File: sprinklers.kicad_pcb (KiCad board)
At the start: 2 copper layers, 144.3 x 152.4 mm, 69 parts, among them J1 Conn_01x02, J2 Conn_01x02, J3 Conn_01x02, J4 Conn_01x02, J5 Conn_01x02, J6 Conn_01x02, K1 SANYOU_SRD_Form_C, K2 SANYOU_SRD_Form_C, K3 SANYOU_SRD_Form_C, K4 SANYOU_SRD_Form_C, K5 SANYOU_SRD_Form_C, K6 SANYOU_SRD_Form_C, Q1 Q_NMOS_GDS, Q2 Q_NMOS_GDS, Q3 Q_NMOS_GDS, Q4 Q_NMOS_GDS, Q5 Q_NMOS_GDS, Q6 Q_NMOS_GDS, U1 LM2596S-5, U2 AP1117-33, U2 ESP32-WROOM-32D, U3 AP1117-33, U3 ESP32-WROOM-32D

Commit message: V1.1.0 with notation
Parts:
- removed 12V-IN, SENSOR: Conn_01x02, Connector:JWT_A3963_1x02_P3.96mm_Vertical
- removed BOOT: SW_SPST, Button_Switch_SMD:SW_Push_1P1T_NO_Vertical_Wuerth_434133025816
- removed the C1 at (105.4, 79.2)
- removed the C1 at (46.0, 147.5)
- removed the C2 at (46.0, 148.7)
- removed the C2 at (106.7, 79.2)
- removed the C3 at (119.4, 78.7)
- removed the C3 at (41.8, 162.4)
- removed the C4 at (120.7, 78.7)
- removed the C4 at (43.1, 162.4)
- removed the C5 at (47.0, 90.6)
- removed the C5 at (27.5, 142.4)
- removed the C6 at (55.9, 84.3)
- removed the C6 at (25.7, 153.5)
- removed the D1 at (128.1, 38.1)
- removed the D1 at (34.1, 132.2)
- removed the D2 at (128.1, 35.6)
- removed the D2 at (33.6, 139.8)
- removed the D3 at (128.1, 33.0)
- removed the D3 at (60.8, 141.1)
- removed the D4 at (58.2, 141.1)
- removed the D4 at (45.7, 80.5)
- removed the D5 at (55.9, 141.1)
- removed the D5 at (55.9, 90.6)
- removed the EXT/PROG at (65.9, 131.0)
- removed the EXT/PROG at (143.5, 66.0)
- removed GND 5V 3V3: PinHeader_1x03_P2.54mm_Vertical, Connector_PinHeader_2.54mm:PinHeader_1x03_P2.54mm_Vertical
- removed the L1 at (37.3, 152.8)
- removed the L1 at (89.5, 88.0)
- removed the R1 at (33.1, 43.2)
- removed the R1 at (60.7, 137.3)
- removed the R2 at (58.3, 137.3)
- removed the R2 at (50.2, 43.2)
- removed the R3 at (55.8, 137.3)
- removed the R3 at (68.6, 43.2)
- removed the R7 at (123.0, 33.0)
- removed the R8 at (123.0, 35.6)
- removed the R9 at (123.0, 38.1)
- removed the U1 at (74.6, 89.1)
- removed the U1 at (43.3, 135.1)
- removed the U2 at (145.4, 42.0)
- removed the U2 at (35.4, 164.0)
- removed the U3 at (113.6, 81.3)
- removed the U3 at (61.4, 154.4)
- added 7  6  5  G: PinHeader_1x04_P2.54mm_Vertical, Connector_PinHeader_2.54mm:PinHeader_1x04_P2.54mm_Vertical, F.Cu at (148.5, 22.8)
- added ?: , , F.Cu at (41.0, 166.8)
- added ?: LOGO, my lib:sprinklers qr code, B.Cu at (40.3, 169.5)
- added ?: LOGO, my lib:sprinklers qr code, B.Cu at (90.2, 38.1)
- added ?: , , F.Cu at (43.5, 166.8)
- added ?: , , F.Cu at (41.0, 124.8)
- added ?: , , F.Cu at (38.4, 166.8)
- added ?: , , F.Cu at (141.0, 65.2)
- added ?: , , F.Cu at (43.5, 124.8)
- added ?: , , F.Cu at (38.5, 124.8)
- added ?: , , F.Cu at (130.7, 25.4)
- added ?: LOGO, my lib:sprinklers qr code, B.Cu at (40.3, 127.4)
- added AC12-IN1: Conn_01x02, Connector:JWT_A3963_1x02_P3.96mm_Vertical, F.Cu at (73.0, 137.6)
- added AC12-IN1: Conn_01x02, Connector:JWT_A3963_1x02_P3.96mm_Vertical, F.Cu at (73.0, 179.6)
- added C1: 10uF, Capacitor_SMD:C_0805_2012Metric, F.Cu at (36.9, 132.5)
- added C1: 10uF, Capacitor_SMD:C_0805_2012Metric, F.Cu at (36.9, 174.5)
- added C1: 10uF, Capacitor_SMD:C_0805_2012Metric, F.Cu at (102.9, 75.5)
- added C2: 100nF, Capacitor_SMD:C_0603_1608Metric, F.Cu at (39.6, 132.5)
- added C2: 100nF, Capacitor_SMD:C_0603_1608Metric, F.Cu at (39.6, 174.5)
- added C2: 100nF, Capacitor_SMD:C_0603_1608Metric, F.Cu at (104.8, 76.2)
- added C3: 10uF, Capacitor_SMD:C_0805_2012Metric, F.Cu at (116.8, 75.7)
- added C3: 10uF, Capacitor_SMD:C_0805_2012Metric, F.Cu at (36.9, 136.6)
- added C3: 10uF, Capacitor_SMD:C_0805_2012Metric, F.Cu at (36.9, 178.7)
- added C4: 100nF, Capacitor_SMD:C_0603_1608Metric, F.Cu at (39.7, 178.7)
- added C4: 100nF, Capacitor_SMD:C_0603_1608Metric, F.Cu at (119.4, 75.1)
- added C4: 100nF, Capacitor_SMD:C_0603_1608Metric, F.Cu at (39.7, 136.7)
- added C5: C_Polarized, Capacitor_THT:CP_Radial_D8.0mm_P3.50mm, F.Cu at (45.7, 88.4)
- added C5: C_Polarized, Capacitor_THT:CP_Radial_D8.0mm_P3.50mm, F.Cu at (73.7, 116.8)
- added C5: C_Polarized, Capacitor_THT:CP_Radial_D8.0mm_P3.50mm, F.Cu at (73.7, 158.8)
- added C6: C_Polarized, Capacitor_THT:CP_Radial_D8.0mm_P3.50mm, F.Cu at (63.6, 167.7)
- added C6: C_Polarized, Capacitor_THT:CP_Radial_D8.0mm_P3.50mm, F.Cu at (53.3, 81.0)
- added C6: C_Polarized, Capacitor_THT:CP_Radial_D8.0mm_P3.50mm, F.Cu at (63.6, 125.7)
- added D1: LED, LED_SMD:LED_0402_1005Metric, F.Cu at (125.6, 34.8)
- added D1: LED, LED_SMD:LED_0402_1005Metric, F.Cu at (27.2, 166.4)
- added D1: LED, LED_SMD:LED_0402_1005Metric, F.Cu at (27.2, 124.4)
- added D2: LED, LED_SMD:LED_0402_1005Metric, F.Cu at (125.6, 32.3)
- added D2: LED, LED_SMD:LED_0402_1005Metric, F.Cu at (33.1, 166.4)
- added D2: LED, LED_SMD:LED_0402_1005Metric, F.Cu at (33.1, 124.4)
- added D3: LED, LED_SMD:LED_0402_1005Metric, F.Cu at (125.6, 29.7)
- added D3: LED, LED_SMD:LED_0402_1005Metric, F.Cu at (29.8, 124.4)
- added D3: LED, LED_SMD:LED_0402_1005Metric, F.Cu at (29.8, 166.4)
- added D4: 900mV@2A 30ns 2A 50V DO-214AA Diodes, Diode_SMD:D_SMB, F.Cu at (63.6, 179.1)
- added D4: 900mV@2A 30ns 2A 50V DO-214AA Diodes, Diode_SMD:D_SMB, F.Cu at (63.6, 137.1)
- added D4: 900mV@2A 30ns 2A 50V DO-214AA Diodes, Diode_SMD:D_SMB, F.Cu at (33.8, 79.2)
- added D5: B140-E3, Diode_SMD:D_SMA, F.Cu at (55.9, 163.2)
- added D5: B140-E3, Diode_SMD:D_SMA, F.Cu at (53.3, 87.3)
- added D5: B140-E3, Diode_SMD:D_SMA, F.Cu at (56.0, 121.1)
- added D6: 900mV@2A 30ns 2A 50V DO-214AA Diodes, Diode_SMD:D_SMB, F.Cu at (33.8, 75.4)
- added D6: 900mV@2A 30ns 2A 50V DO-214AA Diodes, Diode_SMD:D_SMB, F.Cu at (63.6, 173.2)
- added D6: 900mV@2A 30ns 2A 50V DO-214AA Diodes, Diode_SMD:D_SMB, F.Cu at (63.6, 131.1)
- added D7: 900mV@2A 30ns 2A 50V DO-214AA Diodes, Diode_SMD:D_SMB, F.Cu at (70.8, 127.5)
- added D7: 900mV@2A 30ns 2A 50V DO-214AA Diodes, Diode_SMD:D_SMB, F.Cu at (39.4, 84.9)
- added D7: 900mV@2A 30ns 2A 50V DO-214AA Diodes, Diode_SMD:D_SMB, F.Cu at (70.8, 169.5)
- added D8: 900mV@2A 30ns 2A 50V DO-214AA Diodes, Diode_SMD:D_SMB, F.Cu at (76.3, 127.5)
- added D8: 900mV@2A 30ns 2A 50V DO-214AA Diodes, Diode_SMD:D_SMB, F.Cu at (44.5, 81.8)
- added D8: 900mV@2A 30ns 2A 50V DO-214AA Diodes, Diode_SMD:D_SMB, F.Cu at (76.3, 169.5)
- added EXT/PROG: PinHeader_2x03_P1.27mm_Vertical, Connector_PinHeader_1.27mm:PinHeader_2x03_P1.27mm_Vertical, F.Cu at (48.6, 109.6)
- added EXT/PROG: PinHeader_2x03_P1.27mm_Vertical, Connector_PinHeader_1.27mm:PinHeader_2x03_P1.27mm_Vertical, F.Cu at (141.0, 62.7)
- added EXT/PROG: PinHeader_2x03_P1.27mm_Vertical, Connector_PinHeader_1.27mm:PinHeader_2x03_P1.27mm_Vertical, F.Cu at (48.6, 151.6)
- added L1: L, Inductor_SMD:L_12x12mm_H8mm, F.Cu at (61.3, 151.3)
- added L1: L, Inductor_SMD:L_12x12mm_H8mm, F.Cu at (61.3, 109.3)
- added L1: L, Inductor_SMD:L_12x12mm_H8mm, F.Cu at (87.0, 84.7)
- added R1: 1K, Resistor_SMD:R_1206_3216Metric, F.Cu at (30.5, 39.9)
- added R11: 130, Resistor_SMD:R_1206_3216Metric, F.Cu at (130.7, 23.9)
- added R12: 130, Resistor_SMD:R_1206_3216Metric, F.Cu at (133.2, 23.9)
- added R13: 130, Resistor_SMD:R_1206_3216Metric, F.Cu at (135.8, 23.9)
- added R2: 1K, Resistor_SMD:R_1206_3216Metric, F.Cu at (47.7, 39.9)
- added R3: 1K, Resistor_SMD:R_1206_3216Metric, F.Cu at (66.0, 39.9)
- added R7: 130, Resistor_SMD:R_1206_3216Metric, F.Cu at (120.5, 29.7)
- added R7: 130, Resistor_SMD:R_1206_3216Metric, F.Cu at (30.5, 170.3)
- added R7: 130, Resistor_SMD:R_1206_3216Metric, F.Cu at (30.6, 128.2)
- added R8: 130, Resistor_SMD:R_1206_3216Metric, F.Cu at (33.9, 128.2)
- added R8: 130, Resistor_SMD:R_1206_3216Metric, F.Cu at (33.8, 170.3)
- added R8: 130, Resistor_SMD:R_1206_3216Metric, F.Cu at (120.5, 32.3)
- added R9: 130, Resistor_SMD:R_1206_3216Metric, F.Cu at (27.3, 170.3)
- added R9: 130, Resistor_SMD:R_1206_3216Metric, F.Cu at (120.5, 34.8)
- added R9: 130, Resistor_SMD:R_1206_3216Metric, F.Cu at (27.3, 128.2)
- added RV1: R_Potentiometer_Small, Potentiometer_THT:Potentiometer_Bourns_3296Y_Vertical, F.Cu at (127.0, 78.0)
- added RV1: R_Potentiometer_Small, Potentiometer_THT:Potentiometer_Bourns_3296Y_Vertical, F.Cu at (71.5, 147.8)
- added RV1: R_Potentiometer_Small, Potentiometer_THT:Potentiometer_Bourns_3296Y_Vertical, F.Cu at (71.5, 105.7)
- added SENSOR1: Conn_01x02, Connector:JWT_A3963_1x02_P3.96mm_Vertical, F.Cu at (152.8, 79.0)
- added U1: LM2596S-5, Package_TO_SOT_SMD:TO-263-5_TabPin3, F.Cu at (48.6, 132.0)
- added U1: LM2596S-5, Package_TO_SOT_SMD:TO-263-5_TabPin3, F.Cu at (72.0, 85.8)
- added U1: LM2596S-5, Package_TO_SOT_SMD:TO-263-5_TabPin3, F.Cu at (48.6, 174.1)
- added U2: ESP32-WROOM-32D, RF_Module:ESP32-WROOM-32D, F.Cu at (34.4, 153.6)
- added U2: ESP32-WROOM-32D, RF_Module:ESP32-WROOM-32D, F.Cu at (34.5, 111.6)
- added U2: ESP32-WROOM-32D, RF_Module:ESP32-WROOM-32D, F.Cu at (142.9, 38.7)
- added U3: AP1117-33, Package_TO_SOT_SMD:SOT-223-3_TabPin2, F.Cu at (111.1, 78.0)
- added U3: AP1117-33, Package_TO_SOT_SMD:SOT-223-3_TabPin2, F.Cu at (30.5, 177.9)
- added U3: AP1117-33, Package_TO_SOT_SMD:SOT-223-3_TabPin2, F.Cu at (30.6, 135.8)
- moved 26 27 28 29 11.5 mm to (135.2, 50.9), turned to 0 degrees
- moved J1 7.52 mm to (99.3, 87.4)
- moved J2 7.52 mm to (108.9, 87.4)
- moved J3 7.52 mm to (118.5, 87.4)
- moved J4 7.52 mm to (128.1, 87.4)
- moved J5 7.52 mm to (137.7, 87.4)
- moved J6 7.52 mm to (147.3, 87.4)
- moved 5V 3V3 GND 4.18 mm to (143.5, 71.6)
- moved K4 4.17 mm to (89.2, 52.4)
- moved K6 4.17 mm to (124.5, 52.4)
- moved Q3 4.17 mm to (69.4, 44.7)
- moved Q5 4.17 mm to (104.4, 44.7)
- moved K1 4.17 mm to (36.2, 52.4)
- moved K2 4.17 mm to (53.8, 52.4)
- moved Q4 4.17 mm to (86.8, 45.0)
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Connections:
- 26 27 28 29 pad 1: unconnected-(U2-IO5-Pad29) -> (no net)
- 26 27 28 29 pad 2: unconnected-(U2-IO17-Pad28) -> (no net)
- 26 27 28 29 pad 3: unconnected-(U2-IO16-Pad27) -> (no net)
- 26 27 28 29 pad 4: unconnected-(U2-IO4-Pad26) -> (no net)
- 5V 3V3 GND pad 1: GND1 -> (no net)
- 5V 3V3 GND pad 2: Net-(U2-VDD) -> (no net)
- 5V 3V3 GND pad 3: DC5V -> (no net)
- AC24-IN1 pad 2: GND1 -> Net-(AC24-IN1-Pin_2)
- K1 pad 5: DC5V -> Net-(U1-FB)
- K2 pad 5: DC5V -> Net-(U1-FB)
- K3 pad 5: DC5V -> Net-(U1-FB)
- K4 pad 5: DC5V -> Net-(U1-FB)
- K5 pad 5: DC5V -> Net-(U1-FB)
- K6 pad 5: DC5V -> Net-(U1-FB)
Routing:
- net Net-(SENSOR1-Pin_2): track 0.00 -> 566.6 mm, vias 0 -> 22
- net Net-(SENSOR1-Pin_1): track 0.00 -> 445.9 mm, vias 0 -> 24
- net Net-(U1-FB): track 0.00 -> 389.0 mm, vias 0 -> 6
- net DC5V: track 254.9 -> 0.00 mm, vias 2 -> 0
- net Net-(AC24-IN1-Pin_2): track 0.00 -> 183.7 mm
- net GND1: track 896.5 -> 1060.1 mm, vias 1 -> 7
- net Net-(D5-K): track 66.5 -> 222.3 mm
- net (no net): track 358.7 -> 228.4 mm, vias 13 -> 2
- net Net-(D4-K): track 42.5 -> 143.7 mm
- net Net-(U2-VDD): track 95.1 -> 0.00 mm, vias 2 -> 0
- net Net-(D1-A): track 7.62 -> 50.1 mm, vias 0 -> 4
- net Net-(AC12-IN1-Pin_1): track 0.00 -> 35.0 mm
- net Net-(AC12-IN1-Pin_2): track 0.00 -> 20.7 mm
- net Net-(D2-K): track 28.5 -> 8.06 mm, vias 2 -> 0
- net Net-(D1-K): track 28.5 -> 8.21 mm
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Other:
- board size 144.3 x 152.4 mm -> 147.4 x 171.8 mm
- board text added: "<-- V-CUT"
- board text added: "P11"
- board text added: "P12"
- board text added: "TheDontKnowGuy"
- board text added: "These are 2 duplicats of the main board minus the 6x relays."
- board text removed: "GIDEONI"
- board text removed: "GRD AC vs DC https://rayshobby.net/wordpress/24vac-to-5vdc-conversion/"

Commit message: applying fixed after review
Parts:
- removed 26 27 28 29: PinHeader_1x04_P2.54mm_Vertical, Connector_PinHeader_2.54mm:PinHeader_1x04_P2.54mm_Vertical
- removed 5V 3V3 GND: PinHeader_1x03_P2.54mm_Vertical, Connector_PinHeader_2.54mm:PinHeader_1x03_P2.54mm_Vertical
- removed 7  6  5  G: PinHeader_1x04_P2.54mm_Vertical, Connector_PinHeader_2.54mm:PinHeader_1x04_P2.54mm_Vertical
- removed ? (x8): , 
- removed ? (x3): LOGO, my lib:sprinklers qr code
- removed AC12-IN1 (x2): Conn_01x02, Connector:JWT_A3963_1x02_P3.96mm_Vertical
- removed the C1 at (36.9, 132.5)
- removed the C1 at (36.9, 174.5)
- removed the C2 at (39.6, 132.5)
- removed the C2 at (39.6, 174.5)
- removed the C3 at (36.9, 136.6)
- removed the C3 at (36.9, 178.7)
- removed the C4 at (39.7, 178.7)
- removed the C4 at (39.7, 136.7)
- removed the C5 at (73.7, 116.8)
- removed the C5 at (73.7, 158.8)
- removed the C6 at (63.6, 167.7)
- removed the C6 at (63.6, 125.7)
- removed the D1 at (27.2, 166.4)
- removed the D1 at (27.2, 124.4)
- removed the D2 at (33.1, 166.4)
- removed the D2 at (33.1, 124.4)
- removed the D3 at (29.8, 124.4)
- removed the D3 at (29.8, 166.4)
- removed the D4 at (63.6, 179.1)
- removed the D4 at (63.6, 137.1)
- removed the D5 at (55.9, 163.2)
- removed the D5 at (56.0, 121.1)
- removed the D6 at (63.6, 173.2)
- removed the D6 at (63.6, 131.1)
- removed the D7 at (70.8, 127.5)
- removed the D7 at (70.8, 169.5)
- removed the D8 at (76.3, 127.5)
- removed the D8 at (76.3, 169.5)
- removed EXT/PROG (x3): PinHeader_2x03_P1.27mm_Vertical, Connector_PinHeader_1.27mm:PinHeader_2x03_P1.27mm_Vertical
- removed the L1 at (61.3, 151.3)
- removed the L1 at (61.3, 109.3)
- removed the R7 at (30.5, 170.3)
- removed the R7 at (30.6, 128.2)
- removed the R8 at (33.9, 128.2)
- removed the R8 at (33.8, 170.3)
- removed the R9 at (27.3, 170.3)
- removed the R9 at (27.3, 128.2)
- removed the RV1 at (71.5, 147.8)
- removed the RV1 at (71.5, 105.7)
- removed the U1 at (48.6, 132.0)
- removed the U1 at (48.6, 174.1)
- removed the U2 at (34.4, 153.6)
- removed the U2 at (34.5, 111.6)
- removed the U3 at (30.5, 177.9)
- removed the U3 at (30.6, 135.8)
- added C7: 25V 1uF X5R ±10% 0402 Multilayer Ceramic Capacitors MLCC - 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, Capacitor_SMD:C_01005_0402Metric, F.Cu at (64.8, 83.8)
- added C8: 25V 1uF X5R ±10% 0402 Multilayer Ceramic Capacitors MLCC - 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, Capacitor_SMD:C_01005_0402Metric, F.Cu at (74.3, 90.2)
- added D10: 75V 400mW Single 1V@50mA 4ns 150mA SOD-123 Switching Diode 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, Diode_SMD:D_SOD-123, F.Cu at (47.3, 49.4)
- added D11: 75V 400mW Single 1V@50mA 4ns 150mA SOD-123 Switching Diode 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, Diode_SMD:D_SOD-123, F.Cu at (30.6, 49.4)
- added D12: 75V 400mW Single 1V@50mA 4ns 150mA SOD-123 Switching Diode 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, Diode_SMD:D_SOD-123, F.Cu at (80.6, 49.4)
- added D13: 75V 400mW Single 1V@50mA 4ns 150mA SOD-123 Switching Diode 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, Diode_SMD:D_SOD-123, F.Cu at (97.2, 49.4)
- added D14: 75V 400mW Single 1V@50mA 4ns 150mA SOD-123 Switching Diode 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, Diode_SMD:D_SOD-123, F.Cu at (113.8, 49.4)
- added D9: 75V 400mW Single 1V@50mA 4ns 150mA SOD-123 Switching Diode 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, Diode_SMD:D_SOD-123, F.Cu at (63.9, 49.4)
- added EXT1: Conn_01x04_Pin, Connector_PinHeader_2.54mm:PinHeader_1x04_P2.54mm_Vertical, F.Cu at (137.2, 59.7)
- added J11: Conn_01x02_Pin, Connector_PinHeader_2.54mm:PinHeader_1x02_P2.54mm_Vertical, F.Cu at (149.9, 66.8)
- added J8: Conn_01x04_Pin, Connector_PinHeader_2.54mm:PinHeader_1x04_P2.54mm_Vertical, F.Cu at (123.2, 24.1)
- added J9: Conn_01x03_Pin, Connector_PinHeader_2.54mm:PinHeader_1x03_P2.54mm_Vertical, F.Cu at (134.6, 74.9)
- added PROG/EXT1: Conn_01x06_Pin, Connector_PinHeader_2.54mm:PinHeader_1x06_P2.54mm_Vertical, F.Cu at (146.1, 24.1)
- added R10: 10K, Resistor_SMD:R_1206_3216Metric, F.Cu at (137.2, 67.3)
- added REF**: NetTie-2_THT_Pad0.3mm, NetTie:NetTie-2_THT_Pad0.3mm, F.Cu at (139.6, 53.4)
- added SW1: SW_SPST, Button_Switch_SMD:SW_SPST_TL3342, F.Cu at (142.8, 68.0)
- C5, C6: footprint Capacitor_THT:CP_Radial_D8.0mm_P3.50mm -> Capacitor_THT:CP_Radial_D10.0mm_P5.00mm
- R11, R12, R13, R7, R8, R9: footprint Resistor_SMD:R_1206_3216Metric -> Resistor_SMD:R_0201_0603Metric
- moved R7 29.2 mm to (137.2, 53.7), turned to 90 degrees
- moved R8 26.1 mm to (135.3, 53.8), turned to 90 degrees
- moved D3 24.7 mm to (137.2, 51.6), turned to 90 degrees
- moved R9 22.9 mm to (133.3, 53.7), turned to 90 degrees
- moved D2 21.6 mm to (135.3, 51.6), turned to 90 degrees
- moved D1 18.5 mm to (133.3, 51.6), turned to 90 degrees
- moved R13 17.9 mm to (118.4, 28.3)
- moved R12 13.8 mm to (120.2, 28.3)
- moved R1 10.9 mm to (40.9, 43.1), turned to 90 degrees
- moved R2 10.4 mm to (57.6, 43.1), turned to 90 degrees
- moved R11 9.79 mm to (121.9, 28.3)
- moved R3 8.82 mm to (74.2, 43.1), turned to 90 degrees
- moved D7 8.76 mm to (40.6, 76.2)
- moved R4 7.80 mm to (90.9, 43.1), turned to 90 degrees
- moved R5 7.22 mm to (107.6, 43.1), turned to 90 degrees
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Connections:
- net Net-(SENSOR1-Pin_2) renamed 3V3
- net Net-(U1-FB) renamed 5V
- C1 pad 2: GND1 -> GRD
- C2 pad 2: GND1 -> GRD
- C3 pad 2: GND1 -> GRD
- C4 pad 2: GND1 -> GRD
- C5 pad 2: GND1 -> GRD
- C6 pad 2: GND1 -> GRD
- D5 pad 2: GND1 -> GRD
- D6 pad 2: GND1 -> GRD
- D8 pad 2: GND1 -> GRD
- J1 pad 2: GND1 -> Net-(AC24-IN1-Pin_2)
- J2 pad 2: GND1 -> Net-(AC24-IN1-Pin_2)
- J3 pad 2: GND1 -> Net-(AC24-IN1-Pin_2)
- J4 pad 2: GND1 -> Net-(AC24-IN1-Pin_2)
- J5 pad 2: GND1 -> Net-(AC24-IN1-Pin_2)
- J6 pad 2: GND1 -> Net-(AC24-IN1-Pin_2)
- K1 pad 2: Net-(Q1-D) -> Net-(D11-K)
- K1 pad 3: unconnected-(K1-Pad3) -> Net-(J1-Pin_1)
- K1 pad 4: Net-(J1-Pin_1) -> unconnected-(K1-Pad4)
- K2 pad 2: Net-(Q2-D) -> Net-(D10-K)
- K2 pad 3: unconnected-(K2-Pad3) -> Net-(J2-Pin_1)
- K2 pad 4: Net-(J2-Pin_1) -> unconnected-(K2-Pad4)
- K3 pad 2: Net-(Q3-D) -> Net-(D9-K)
- K3 pad 3: unconnected-(K3-Pad3) -> Net-(J3-Pin_1)
- K3 pad 4: Net-(J3-Pin_1) -> unconnected-(K3-Pad4)
- K4 pad 2: Net-(Q4-D) -> Net-(D12-K)
- K4 pad 3: unconnected-(K4-Pad3) -> Net-(J4-Pin_1)
- K4 pad 4: Net-(J4-Pin_1) -> unconnected-(K4-Pad4)
- K5 pad 2: Net-(Q5-D) -> Net-(D13-K)
- K5 pad 3: unconnected-(K5-Pad3) -> Net-(J5-Pin_1)
- K5 pad 4: Net-(J5-Pin_1) -> unconnected-(K5-Pad4)
- K6 pad 2: Net-(Q6-D) -> Net-(D14-K)
- K6 pad 3: unconnected-(K6-Pad3) -> Net-(J6-Pin_1)
- K6 pad 4: Net-(J6-Pin_1) -> unconnected-(K6-Pad4)
- Q1 pad 2: Net-(Q1-D) -> Net-(D11-A)
- Q1 pad 3: GND1 -> GRD
- Q2 pad 2: Net-(Q2-D) -> Net-(D10-A)
- Q2 pad 3: GND1 -> GRD
- Q3 pad 2: Net-(Q3-D) -> Net-(D9-A)
- Q3 pad 3: GND1 -> GRD
- Q4 pad 2: Net-(Q4-D) -> Net-(D12-A)
- Q4 pad 3: GND1 -> GRD
- Q5 pad 2: Net-(Q5-D) -> Net-(D13-A)
- Q5 pad 3: GND1 -> GRD
- Q6 pad 2: Net-(Q6-D) -> Net-(D14-A)
- Q6 pad 3: GND1 -> GRD
- R1 pad 2: Net-(U2-IO26) -> GRD
- R11 pad 1: (no net) -> Net-(J8-Pin_1)
- R11 pad 2: unconnected-(U2-IO35-Pad7) -> Net-(U2-IO13)
- R12 pad 1: (no net) -> Net-(J8-Pin_2)
- R12 pad 2: unconnected-(U2-IO34-Pad6) -> Net-(U2-IO5)
- R13 pad 1: (no net) -> Net-(J8-Pin_3)
- R13 pad 2: unconnected-(U2-SENSOR_VN-Pad5) -> Net-(U2-IO4)
- R2 pad 2: Net-(U2-IO14) -> GRD
- R3 pad 2: Net-(U2-IO12) -> GRD
- R4 pad 2: Net-(U2-IO13) -> GRD
- R5 pad 2: Net-(U2-SCS/CMD) -> GRD
- R6 pad 2: Net-(U2-SDO/SD0) -> GRD
- R7 pad 1: GND1 -> GRD
- R8 pad 1: GND1 -> GRD
- R9 pad 1: GND1 -> GRD
- RV1 pad 1: GND1 -> GRD
- U1 pad 3: GND1 -> GRD
- U1 pad 5: GND1 -> GRD
- U2 pad 1: GND1 -> GRD
- U2 pad 10: Net-(D3-A) -> Net-(Q2-G)
- U2 pad 11: Net-(U2-IO26) -> Net-(Q3-G)
- U2 pad 12: unconnected-(U2-IO27-Pad12) -> Net-(Q4-G)
- U2 pad 13: Net-(U2-IO14) -> Net-(Q5-G)
- U2 pad 14: Net-(U2-IO12) -> Net-(Q6-G)
- U2 pad 15: GND1 -> GRD
- U2 pad 17: Net-(D1-A) -> unconnected-(U2-SHD/SD2-Pad17)
- U2 pad 19: Net-(U2-SCS/CMD) -> unconnected-(U2-SCS/CMD-Pad19)
- U2 pad 21: Net-(U2-SDO/SD0) -> unconnected-(U2-SDO/SD0-Pad21)
- U2 pad 23: unconnected-(U2-IO15-Pad23) -> Net-(D1-A)
- U2 pad 25: unconnected-(U2-IO0-Pad25) -> Net-(PROG/EXT1-Pin_3)
- U2 pad 26: unconnected-(U2-IO4-Pad26) -> Net-(U2-IO4)
- U2 pad 27: unconnected-(U2-IO16-Pad27) -> Net-(D2-A)
- U2 pad 28: unconnected-(U2-IO17-Pad28) -> Net-(D3-A)
- U2 pad 29: unconnected-(U2-IO5-Pad29) -> Net-(U2-IO5)
- U2 pad 3: unconnected-(U2-EN-Pad3) -> Net-(J11-Pin_1)
- U2 pad 33: unconnected-(U2-IO21-Pad33) -> Net-(Q1-G)
- U2 pad 34: unconnected-(U2-RXD0/IO3-Pad34) -> Net-(PROG/EXT1-Pin_4)
- U2 pad 35: unconnected-(U2-TXD0/IO1-Pad35) -> Net-(PROG/EXT1-Pin_5)
- U2 pad 36: unconnected-(U2-IO22-Pad36) -> Net-(EXT1-Pin_3)
- U2 pad 37: unconnected-(U2-IO23-Pad37) -> Net-(EXT1-Pin_4)
- U2 pad 38: GND1 -> GRD
- U2 pad 39: GND1 -> GRD
- U2 pad 6: unconnected-(U2-IO34-Pad6) -> Net-(SENSOR1-Pin_1)
- U2 pad 7: unconnected-(U2-IO35-Pad7) -> Net-(EXT1-Pin_1)
- U2 pad 8: Net-(D2-A) -> Net-(EXT1-Pin_2)
- U2 pad 9: Net-(SENSOR1-Pin_1) -> unconnected-(U2-IO33-Pad9)
- U3 pad 1: GND1 -> GRD
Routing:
- net GND1: track 1060.1 -> 0.00 mm, vias 7 -> 0
- net 3V3: track 566.6 -> 122.4 mm, vias 22 -> 1
- net GRD: track 0.00 -> 419.4 mm, vias 0 -> 3
- net Net-(SENSOR1-Pin_1): track 445.9 -> 78.8 mm, vias 24 -> 1
- net (no net): track 228.4 -> 0.00 mm, vias 2 -> 0
- net Net-(D5-K): track 222.3 -> 24.1 mm, vias 2 -> 0
- net 5V: track 389.0 -> 213.6 mm, vias 6 -> 1
- net Net-(Q1-G): track 3.14 -> 125.5 mm
- net Net-(U2-IO26): track 118.2 -> 0.00 mm, vias 2 -> 0
- net Net-(D4-K): track 143.7 -> 35.9 mm
- net Net-(U2-IO14): track 98.1 -> 0.00 mm, vias 2 -> 0
- net Net-(Q2-G): track 3.02 -> 92.2 mm, vias 0 -> 2
- net Net-(J11-Pin_1): track 0.00 -> 85.1 mm
- net Net-(U2-IO12): track 77.1 -> 0.00 mm, vias 2 -> 0
- net Net-(Q4-G): track 2.90 -> 56.4 mm, vias 0 -> 2
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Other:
- board size 147.4 x 171.8 mm -> 147.3 x 78.7 mm
- board text removed: "+3V3"
- board text removed: "BOOT"
- board text removed: "EN"
- board text removed: "GND"
- board text removed: "MOISTURE SENSOR"
- board text removed: "P11"
- board text removed: "P12"
- board text removed: "R. ${REVISION}"
- board text removed: "RX"
- board text removed: "SPRINKLERS CONTROLLER"
- board text removed: "TX"
- board text removed: "TheDontKnowGuy"
- board text removed: "These are 2 duplicats of the main board minus the 6x relays."

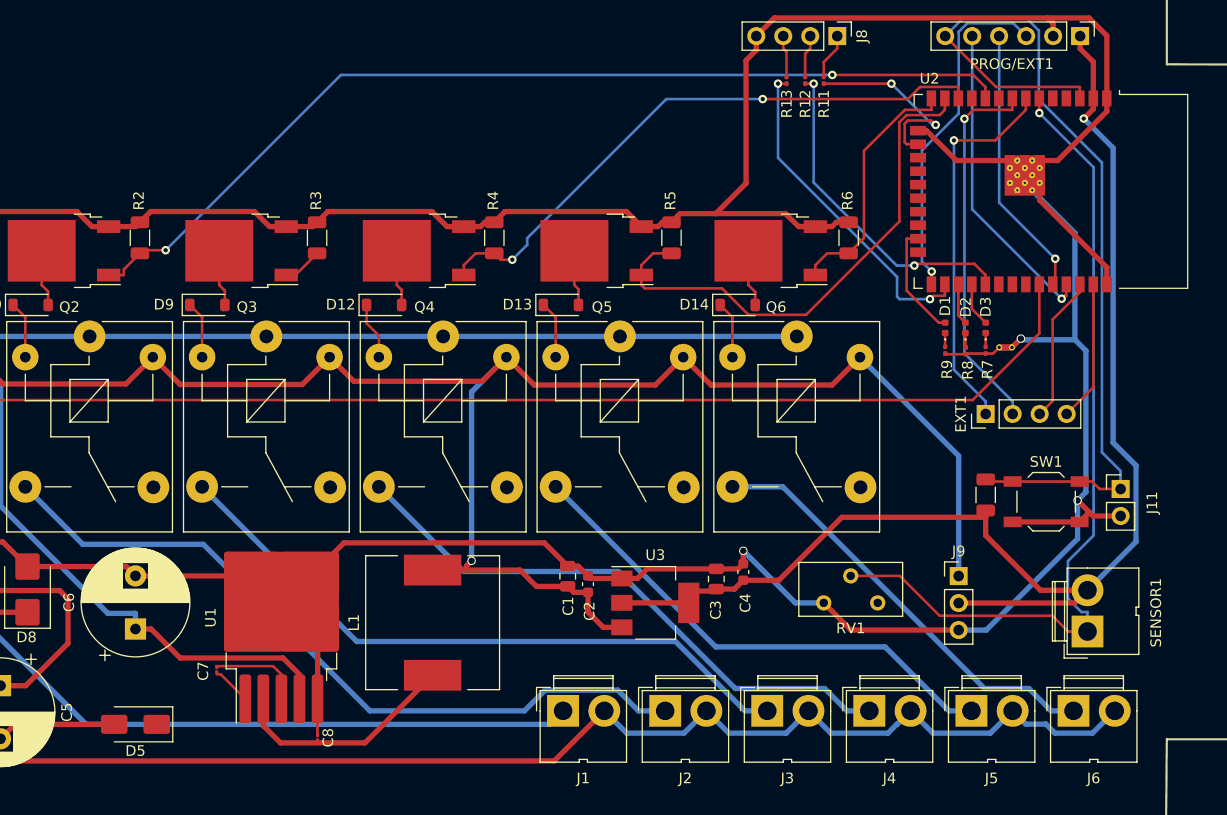
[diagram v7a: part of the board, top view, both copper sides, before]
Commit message: fix capacitor and connect q3
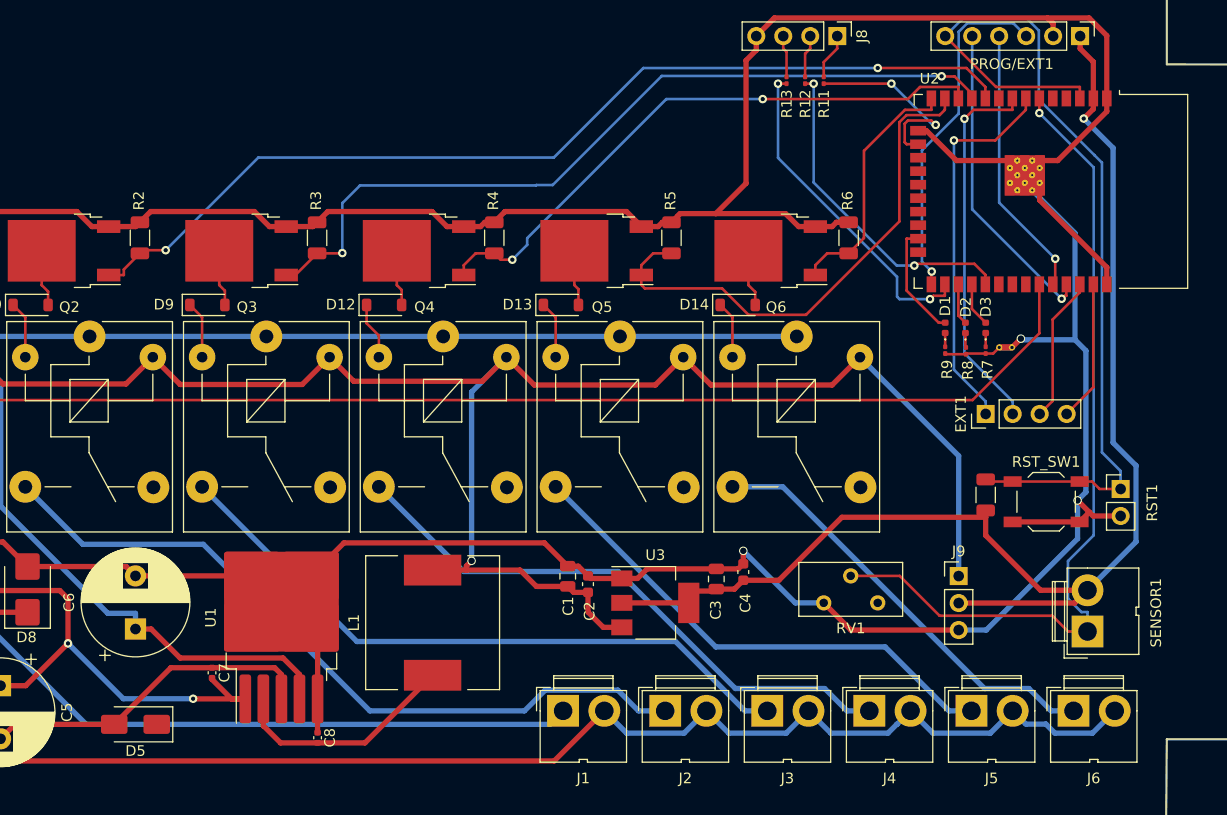
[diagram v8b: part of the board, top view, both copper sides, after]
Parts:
- C7, C8: footprint Capacitor_SMD:C_01005_0402Metric -> Capacitor_SMD:C_0402_1005Metric
- moved C7 0.53 mm to (64.4, 84.1)
- renumbered J11 to RST1, SW1 to RST_SW1
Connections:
- PROG/EXT1 pad 6: Net-(J11-Pin_1) -> Net-(PROG/EXT1-Pin_6)
- R10 pad 2: Net-(J11-Pin_1) -> Net-(PROG/EXT1-Pin_6)
- U2 pad 3: Net-(J11-Pin_1) -> Net-(PROG/EXT1-Pin_6)
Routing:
- net Net-(Q3-G): track 3.75 -> 76.6 mm, vias 0 -> 2
- net Net-(D4-K): track 35.9 -> 55.3 mm, vias 0 -> 2
- net GRD: track 419.4 -> 431.2 mm
- net Net-(Q2-G): track 92.2 -> 92.7 mm
